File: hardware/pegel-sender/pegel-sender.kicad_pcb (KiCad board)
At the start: 2 copper layers, 100 x 70 mm, 90 parts, among them J1 SOLAR / 12V, J2 AKKU 3,2V, J3 SONDE V+ V- A B, J4 HEIZ NTC, J5 XIAO D0-D6, J6 XIAO 5V-D7, Q1 AO3401A, Q2 2N7002, Q3 2N7002, Q4 HL2310A, Q5 AO3401A, Q6 2N7002, Q7 AO3401A, Q8 2N7002, U1 TPS5430, U2 LM324, U3 HT7550-1, U4 CJ431, U5 TPS61040, U6 SP3485EN

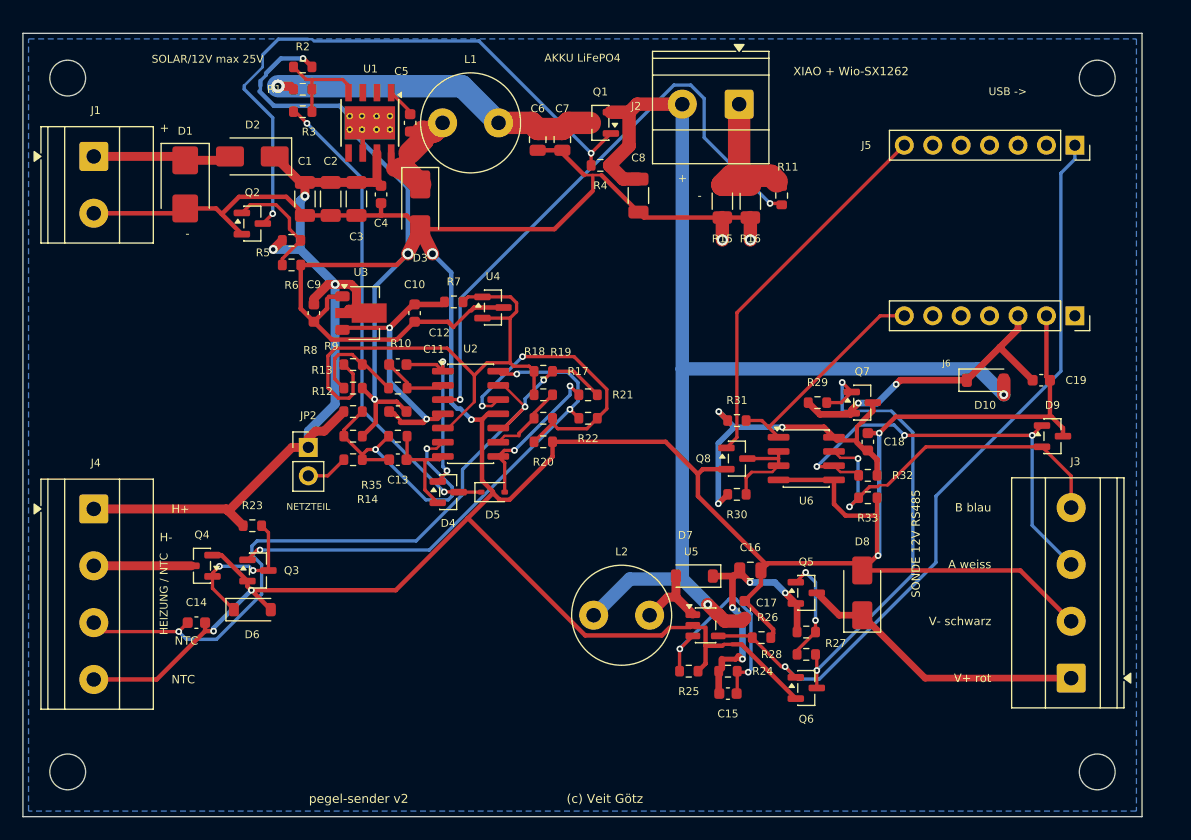
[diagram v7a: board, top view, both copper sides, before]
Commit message: hardware: stable charger without battery, quiet panel regulation in weak light
The simulation now models the TPS5430 with its datasheet type-III
compensation (and OVP) and the LM324 with slew rate. That showed ~10 deg
phase margin of the charger loop without battery and the panel voltage
swinging by +-2.8 V at 5-10 % light. C22 (220 uF with ESR at the charger
output, as in TI's reference design) and C23 (220 uF at the panel) fix
both; TI's all-ceramic network made the panel loop oscillate and is not
used. R7 1k so the CJ431 always gets its 1 mA. Tracks keep 0.5 mm from
the board edge.
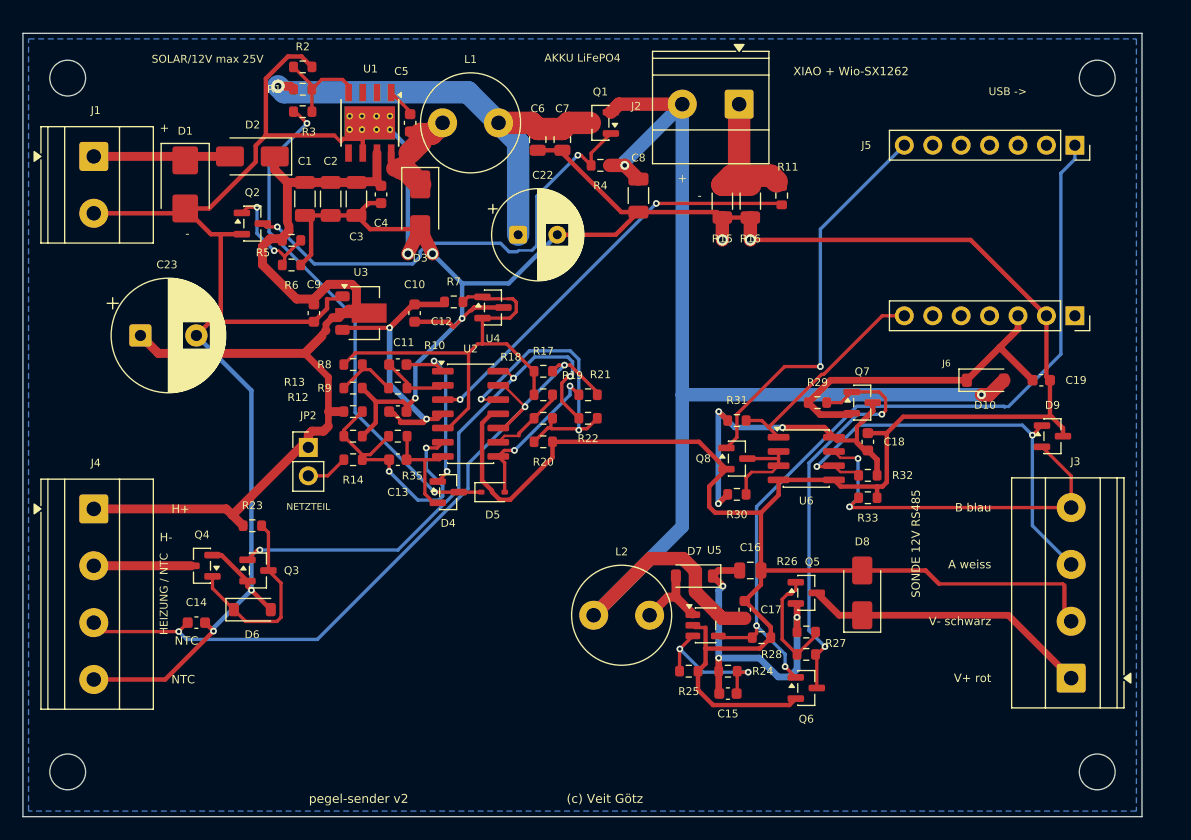
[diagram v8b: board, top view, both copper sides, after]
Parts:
- added C22: 220uF 16V, Capacitor_THT:CP_Radial_D8.0mm_P3.50mm, F.Cu at (94.2, 68.0)
- added C23: 220uF 50V, Capacitor_THT:CP_Radial_D10.0mm_P5.00mm, F.Cu at (60.5, 77.0)
- R7: value 2.2k -> 1k
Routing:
- net CC_SENSE: track 53.7 -> 37.6 mm
- net VSOL: track 79.4 -> 93.3 mm, vias 3 -> 0
- net CHG_PG: track 54.9 -> 42.3 mm
- net CHG_OUT: track 31.2 -> 41.9 mm
- net VREF: track 50.6 -> 40.4 mm
- net VSYS: track 105.2 -> 114.5 mm
- net BST_FB: track 20.8 -> 13.7 mm
- net GND: track 434.7 -> 428.6 mm, vias 11 -> 8
- net PSW_PD: track 41.4 -> 37.0 mm
- net V12_RAW: track 24.5 -> 28.9 mm, vias 4 -> 3
- net SENS_EN: track 69.1 -> 73.1 mm, vias 1 -> 2
- net HEAT_G: track 13.7 -> 17.5 mm, vias 2 -> 0
- net CC_SET: track 9.19 -> 5.82 mm
- net XIAO_3V3: track 27.9 -> 31.2 mm, vias 2 -> 0
- net CHG_LIM: track 43.0 -> 46.3 mm
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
